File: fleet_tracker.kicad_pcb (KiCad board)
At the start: 2 copper layers, 80 x 70 mm, 21 parts, among them J1 DB128V-5.08-5P-GN-S, J2 2685Y-116CNG1SNA01, J3 2685Y-116CNG1SNA01, U2 TJA1051T/3/1J, U3 TSR 1-2450E

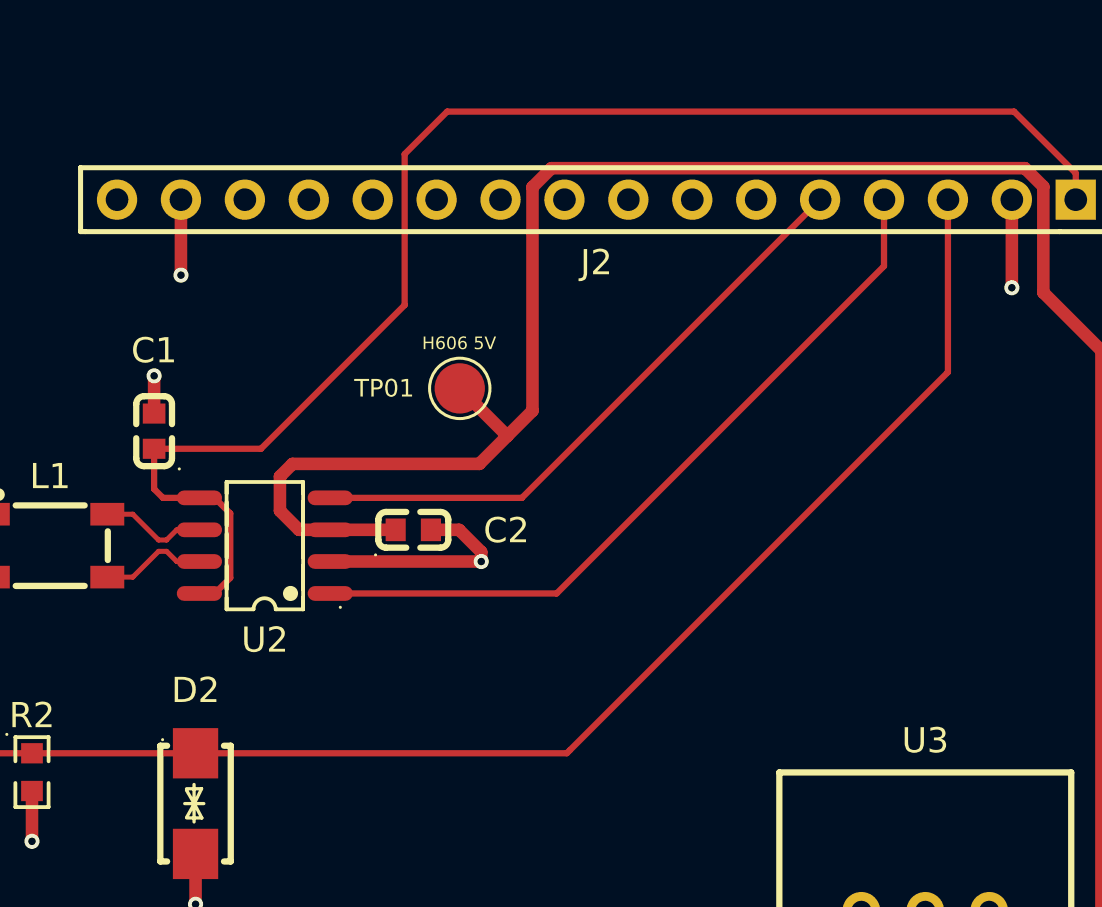
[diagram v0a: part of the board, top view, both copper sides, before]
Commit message: Post-cleanup: co-linear tracks merged, redundant vias removed
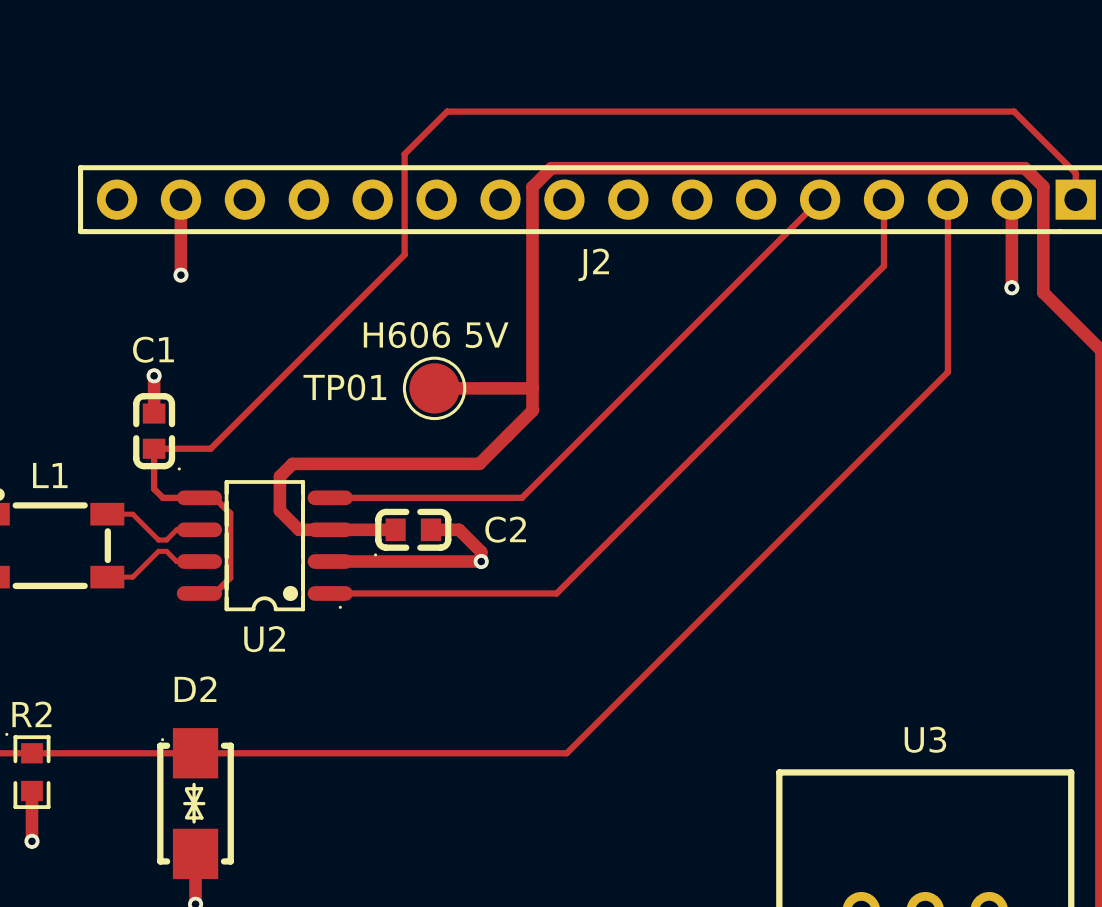
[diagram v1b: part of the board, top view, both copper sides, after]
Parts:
- moved TP01 1.00 mm to (142.5, 114.0)
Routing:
- net /+5V: track 90.4 -> 91.6 mm
- net +3.3V: track 56.8 -> 55.7 mm
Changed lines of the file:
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@@
 	(footprint "TestPoint:TestPoint_Pad_D2.0mm"
 		(layer "F.Cu")
-		(at 143.5 114)
+		(at 142.5 114)
 		(descr "SMD pad as test Point, diameter 2.0mm")
 		(tags "test point SMD pad")
 		(property "Reference" "TP01"
-			(at -3 0 0)
+			(at -3.5 0 0)
 			(layer "F.SilkS")
 			(effects
 				(font
-					(size 0.7 0.7)
-					(thickness 0.0875)
+					(size 1 1)
+					(thickness 0.125)
 				)
 			)
@@
 	)
 	(gr_text "H606 5V"
-		(at 142 112.5 0)
+		(at 142.5 112.5 0)
 		(layer "F.SilkS")
 		(effects
 			(font
-				(size 0.5 0.5)
-				(thickness 0.0625)
+				(size 1 1)
+				(thickness 0.15)
 			)
-			(justify left bottom)
+			(justify bottom)
 		)
 	)
@@
 	)
 	(segment
-		(start 167.98 105.45)
-		(end 165.53 103)
-		(width 0.25)
-		(layer "F.Cu")
-		(net 1)
-	)
-	(segment
-		(start 141.31 104.69)
-		(end 141.31 110.69)
+		(start 167.98 106.5)
+		(end 167.98 105.45)
 		(width 0.25)
 		(layer "F.Cu")
@@
 	)
 	(segment
-		(start 133.759749 122.15)
-		(end 134.379749 121.53)
+		(start 165.53 103)
+		(end 143 103)
 		(width 0.25)
 		(layer "F.Cu")
@@
 	)
 	(segment
-		(start 141.31 110.69)
-		(end 135.6 116.4)
+		(start 133.759749 122.15)
+		(end 134.379749 121.53)
 		(width 0.25)
 		(layer "F.Cu")
@@
 	)
 	(segment
-		(start 167.98 106.5)
-		(end 167.98 105.45)
+		(start 141.31 108.69)
+		(end 133.6 116.4)
 		(width 0.25)
 		(layer "F.Cu")
@@
 	)
 	(segment
-		(start 165.53 103)
-		(end 143 103)
+		(start 141.31 104.69)
+		(end 141.31 108.69)
 		(width 0.25)
 		(layer "F.Cu")
@@
 	)
 	(segment
+		(start 133.6 116.4)
+		(end 131.353749 116.4)
+		(width 0.25)
+		(layer "F.Cu")
+		(net 1)
+	)
+	(segment
 		(start 133.759749 118.35)
 		(end 133.153749 118.35)
@@
 	)
 	(segment
-		(start 133.153749 118.35)
-		(end 131.703749 118.35)
+		(start 167.98 105.45)
+		(end 165.53 103)
 		(width 0.25)
 		(layer "F.Cu")
@@
 	)
 	(segment
-		(start 135.6 116.4)
-		(end 131.353749 116.4)
+		(start 133.153749 118.35)
+		(end 131.703749 118.35)
 		(width 0.25)
 		(layer "F.Cu")
@@
 	)
 	(segment
+		(start 142.5 114)
+		(end 146.39 114)
+		(width 0.5)
+		(layer "F.Cu")
+		(net 3)
+	)
+	(segment
 		(start 169 136.5)
 		(end 167 138.5)
@@
 	)
 	(segment
-		(start 145.39 115.89)
-		(end 143.5 114)
+		(start 146.39 114.89)
+		(end 146.39 114)
 		(width 0.5)
 		(layer "F.Cu")
@@
 	)
 	(segment
-		(start 146.39 114.89)
+		(start 146.39 114)
 		(end 146.39 106.000818)
 		(width 0.5)
@@
 	)
 	(segment
-		(start 147.877293 128.377293)
+		(start 147.754586 128.5)
 		(end 162.9 113.354587)
 		(width 0.25)
@@
 	)
 	(segment
-		(start 147.754586 128.5)
-		(end 147.877293 128.377293)
-		(width 0.25)
-		(layer "F.Cu")
-		(net 5)
-	)
-	(segment
 		(start 113 124.08)
 		(end 117.629999 119.450001)
@@
 		(name "$teardrop_padvia$")
 		(hatch none 0.1)
-		(priority 30009)
+		(priority 30006)
 		(attr
 			(teardrop
@@
 		(polygon
 			(pts
-				(xy 121.553749 122.405764) (xy 121.053749 122.405764) (xy 121.009513 122.941473) (xy 121.303749 123.001)
-				(xy 121.597985 122.941473)
+				(xy 162.594236 144.25) (xy 162.594236 143.75) (xy 162.058527 143.705764) (xy 161.999 144) (xy 162.058527 144.294236)
 			)
 		)
@@
 		(name "$teardrop_padvia$")
 		(hatch none 0.1)
-		(priority 30003)
+		(priority 30010)
 		(attr
 			(teardrop
@@
 		(polygon
 			(pts
-				(xy 152.25 148.405764) (xy 151.75 148.405764) (xy 151.705764 148.941473) (xy 152 149.001) (xy 152.294236 148.941473)
+				(xy 165.69 109.405764) (xy 165.19 109.405764) (xy 165.145764 109.941473) (xy 165.44 110.001) (xy 165.734236 109.941473)
 			)
 		)
@@
 		(name "$teardrop_padvia$")
 		(hatch none 0.1)
-		(priority 30010)
+		(priority 30012)
 		(attr
 			(teardrop
@@
 		(polygon
 			(pts
-				(xy 165.69 109.405764) (xy 165.19 109.405764) (xy 165.145764 109.941473) (xy 165.44 110.001) (xy 165.734236 109.941473)
+				(xy 132.67 89.405764) (xy 132.17 89.405764) (xy 132.125764 89.941473) (xy 132.42 90.001) (xy 132.714236 89.941473)
 			)
 		)
@@
 		(name "$teardrop_padvia$")
 		(hatch none 0.1)
-		(priority 30006)
+		(priority 30007)
 		(attr
 			(teardrop
@@
 		(polygon
 			(pts
-				(xy 162.594236 144.25) (xy 162.594236 143.75) (xy 162.058527 143.705764) (xy 161.999 144) (xy 162.058527 144.294236)
+				(xy 162.25 143.405764) (xy 161.75 143.405764) (xy 161.705764 143.941473) (xy 162 144.001) (xy 162.294236 143.941473)
 			)
 		)
@@
 		(name "$teardrop_padvia$")
 		(hatch none 0.1)
-		(priority 30011)
+		(priority 30000)
 		(attr
 			(teardrop
@@
 		(polygon
 			(pts
-				(xy 132.67 108.905764) (xy 132.17 108.905764) (xy 132.125764 109.441473) (xy 132.42 109.501) (xy 132.714236 109.441473)
+				(xy 126.75 131.405764) (xy 126.25 131.405764) (xy 126.205764 131.941473) (xy 126.5 132.001) (xy 126.794236 131.941473)
 			)
 		)
@@
 		(name "$teardrop_padvia$")
 		(hatch none 0.1)
-		(priority 30001)
+		(priority 30009)
 		(attr
 			(teardrop
@@
 		(polygon
 			(pts
-				(xy 133.25 133.905764) (xy 132.75 133.905764) (xy 132.705764 134.441473) (xy 133 134.501) (xy 133.294236 134.441473)
+				(xy 121.553749 122.405764) (xy 121.053749 122.405764) (xy 121.009513 122.941473) (xy 121.303749 123.001)
+				(xy 121.597985 122.941473)
 			)
 		)
@@
 		(name "$teardrop_padvia$")
 		(hatch none 0.1)
-		(priority 30008)
+		(priority 30004)
 		(attr
 			(teardrop
@@
 		(polygon
 			(pts
-				(xy 143.759513 120.63) (xy 143.759513 121.13) (xy 144.295222 121.174236) (xy 144.354749 120.88)
-				(xy 144.295222 120.585764)
+				(xy 131.103749 114.094236) (xy 131.603749 114.094236) (xy 131.647985 113.558527) (xy 131.353749 113.499)
+				(xy 131.059513 113.558527)
 			)
 		)
@@
 		(name "$teardrop_padvia$")
 		(hatch none 0.1)
-		(priority 30004)
+		(priority 30008)
 		(attr
 			(teardrop
@@
 		(polygon
 			(pts
-				(xy 131.103749 114.094236) (xy 131.603749 114.094236) (xy 131.647985 113.558527) (xy 131.353749 113.499)
-				(xy 131.059513 113.558527)
+				(xy 143.759513 120.63) (xy 143.759513 121.13) (xy 144.295222 121.174236) (xy 144.354749 120.88)
+				(xy 144.295222 120.585764)
 			)
 		)
@@
 		(name "$teardrop_padvia$")
 		(hatch none 0.1)
-		(priority 30007)
+		(priority 30003)
 		(attr
 			(teardrop
@@
 		(polygon
 			(pts
-				(xy 162.25 143.405764) (xy 161.75 143.405764) (xy 161.705764 143.941473) (xy 162 144.001) (xy 162.294236 143.941473)
+				(xy 152.25 148.405764) (xy 151.75 148.405764) (xy 151.705764 148.941473) (xy 152 149.001) (xy 152.294236 148.941473)
 			)
 		)
@@
 		(name "$teardrop_padvia$")
 		(hatch none 0.1)
-		(priority 30013)
+		(priority 30001)
 		(attr
 			(teardrop
@@
 		(polygon
 			(pts
-				(xy 144.379037 120.171736) (xy 144.025485 120.525288) (xy 144.059513 120.938527) (xy 144.354456 120.880707)
-				(xy 144.647985 120.821473)
+				(xy 133.25 133.905764) (xy 132.75 133.905764) (xy 132.705764 134.441473) (xy 133 134.501) (xy 133.294236 134.441473)
 			)
 		)
@@
 		(name "$teardrop_padvia$")
 		(hatch none 0.1)
-		(priority 30012)
+		(priority 30013)
 		(attr
 			(teardrop
@@
 		(polygon
 			(pts
-				(xy 132.67 89.405764) (xy 132.17 89.405764) (xy 132.125764 89.941473) (xy 132.42 90.001) (xy 132.714236 89.941473)
+				(xy 144.379037 120.171736) (xy 144.025485 120.525288) (xy 144.059513 120.938527) (xy 144.354456 120.880707)
+				(xy 144.647985 120.821473)
 			)
 		)
@@
 		(net_name "GND")
 		(layer "F.Cu")
-		(hatch edge 0.5)
-		(connect_pads
-			(clearance 0.5)
+		(name "$teardrop_padvia$")
+		(hatch none 0.1)
+		(priority 30011)
+		(attr
+			(teardrop
+				(type padvia)
+			)
 		)
-		(min_thickness 0.25)
+		(connect_pads yes
+			(clearance 0)
+		)
+		(min_thickness 0.0254)
 		(filled_areas_thickness no)
 		(fill yes
 			(thermal_gap 0.5)
 			(thermal_bridge_width 0.5)
+			(island_removal_mode 1)
+			(island_area_min 10)
 		)
 		(polygon
 			(pts
-				(xy 185 80) (xy 105 80) (xy 105 150) (xy 185 150)
+				(xy 132.67 108.905764) (xy 132.17 108.905764) (xy 132.125764 109.441473) (xy 132.42 109.501) (xy 132.714236 109.441473)
 			)
 		)
@@
 		(net_name "GND")
 		(layer "F.Cu")
-		(name "$teardrop_padvia$")
-		(hatch none 0.1)
-		(priority 30000)
-		(attr
-			(teardrop
-				(type padvia)
-			)
-		)
-		(connect_pads yes
-			(clearance 0)
+		(hatch edge 0.5)
+		(connect_pads
+			(clearance 0.5)
 		)
-		(min_thickness 0.0254)
+		(min_thickness 0.25)
 		(filled_areas_thickness no)
 		(fill yes
 			(thermal_gap 0.5)
 			(thermal_bridge_width 0.5)
-			(island_removal_mode 1)
-			(island_area_min 10)
 		)
 		(polygon
 			(pts
-				(xy 126.75 131.405764) (xy 126.25 131.405764) (xy 126.205764 131.941473) (xy 126.5 132.001) (xy 126.794236 131.941473)
+				(xy 185 80) (xy 105 80) (xy 105 150) (xy 185 150)
 			)
 		)

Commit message: pcb: add silkscren labels for j1
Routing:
- net +3.3V: track 55.7 -> 54.8 mm
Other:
- board text added: "+24V"
- board text added: "CAN_H"
- board text added: "CAN_L"
- board text added: "GND"
- board text added: "IGN"
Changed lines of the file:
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@@
 		(at 113 124.08 -90)
 		(property "Reference" "J1"
-			(at 0.92 6.5 90)
+			(at -14.08 0 0)
 			(layer "F.SilkS")
 			(effects
@@
 		(layer "Edge.Cuts")
 	)
+	(gr_text "IGN"
+		(at 107 129.16 90)
+		(layer "F.SilkS")
+		(effects
+			(font
+				(size 1 1)
+				(thickness 0.1)
+			)
+			(justify bottom)
+		)
+	)
+	(gr_text "CAN_L"
+		(at 107 119 90)
+		(layer "F.SilkS")
+		(effects
+			(font
+				(size 1 1)
+				(thickness 0.1)
+			)
+			(justify bottom)
+		)
+	)
+	(gr_text "CAN_H"
+		(at 107 124.08 90)
+		(layer "F.SilkS")
+		(effects
+			(font
+				(size 1 1)
+				(thickness 0.1)
+			)
+			(justify bottom)
+		)
+	)
 	(gr_text "H606 5V"
 		(at 142.5 112.5 0)
@@
 				(size 1 1)
 				(thickness 0.15)
+			)
+			(justify bottom)
+		)
+	)
+	(gr_text "GND"
+		(at 107 113.92 90)
+		(layer "F.SilkS")
+		(effects
+			(font
+				(size 1 1)
+				(thickness 0.1)
 			)
 			(justify bottom)
@@
 		)
 	)
+	(gr_text "+24V"
+		(at 107 134.24 90)
+		(layer "F.SilkS")
+		(effects
+			(font
+				(size 1 1)
+				(thickness 0.1)
+			)
+			(justify bottom)
+		)
+	)
 	(gr_text "XCOPE AI"
 		(at 109.5 109 90)
@@
 	)
 	(segment
-		(start 143 103)
-		(end 141.31 104.69)
+		(start 141.31 108.69)
+		(end 133.6 116.4)
+		(width 0.25)
+		(layer "F.Cu")
+		(net 1)
+	)
+	(segment
+		(start 131.703749 118.35)
+		(end 131.353749 118)
+		(width 0.25)
+		(layer "F.Cu")
+		(net 1)
+	)
+	(segment
+		(start 133.759749 122.15)
+		(end 134.379749 121.53)
 		(width 0.25)
 		(layer "F.Cu")
@@
 	)
 	(segment
-		(start 131.703749 118.35)
-		(end 131.353749 118)
-		(width 0.25)
-		(layer "F.Cu")
-		(net 1)
-	)
-	(segment
-		(start 165.53 103)
-		(end 143 103)
-		(width 0.25)
-		(layer "F.Cu")
-		(net 1)
-	)
-	(segment
-		(start 133.759749 122.15)
-		(end 134.379749 121.53)
-		(width 0.25)
-		(layer "F.Cu")
-		(net 1)
-	)
-	(segment
 		(start 131.353749 118)
 		(end 131.353749 116.4)
@@
 	)
 	(segment
-		(start 141.31 108.69)
-		(end 133.6 116.4)
+		(start 167.98 105.45)
+		(end 166.53 104)
+		(width 0.25)
+		(layer "F.Cu")
+		(net 1)
+	)
+	(segment
+		(start 142 104)
+		(end 141.31 104.69)
+		(width 0.25)
+		(layer "F.Cu")
+		(net 1)
+	)
+	(segment
+		(start 134.379749 121.53)
+		(end 134.379749 118.97)
 		(width 0.25)
 		(layer "F.Cu")
@@
 	)
 	(segment
-		(start 134.379749 121.53)
-		(end 134.379749 118.97)
+		(start 133.759749 118.35)
+		(end 133.153749 118.35)
+		(width 0.25)
+		(layer "F.Cu")
+		(net 1)
+	)
+	(segment
+		(start 133.153749 122.15)
+		(end 133.759749 122.15)
+		(width 0.25)
+		(layer "F.Cu")
+		(net 1)
+	)
+	(segment
+		(start 133.153749 118.35)
+		(end 131.703749 118.35)
+		(width 0.25)
+		(layer "F.Cu")
+		(net 1)
+	)
+	(segment
+		(start 166.53 104)
+		(end 142 104)
 		(width 0.25)
 		(layer "F.Cu")
@@
 		(start 133.6 116.4)
 		(end 131.353749 116.4)
-		(width 0.25)
-		(layer "F.Cu")
-		(net 1)
-	)
-	(segment
-		(start 133.759749 118.35)
-		(end 133.153749 118.35)
-		(width 0.25)
-		(layer "F.Cu")
-		(net 1)
-	)
-	(segment
-		(start 133.153749 122.15)
-		(end 133.759749 122.15)
-		(width 0.25)
-		(layer "F.Cu")
-		(net 1)
-	)
-	(segment
-		(start 167.98 105.45)
-		(end 165.53 103)
-		(width 0.25)
-		(layer "F.Cu")
-		(net 1)
-	)
-	(segment
-		(start 133.153749 118.35)
-		(end 131.703749 118.35)
 		(width 0.25)
 		(layer "F.Cu")
@@
 		(name "$teardrop_padvia$")
 		(hatch none 0.1)
-		(priority 30006)
+		(priority 30003)
 		(attr
 			(teardrop
@@
 		(polygon
 			(pts
-				(xy 162.594236 144.25) (xy 162.594236 143.75) (xy 162.058527 143.705764) (xy 161.999 144) (xy 162.058527 144.294236)
+				(xy 152.25 148.405764) (xy 151.75 148.405764) (xy 151.705764 148.941473) (xy 152 149.001) (xy 152.294236 148.941473)
 			)
 		)
@@
 		(name "$teardrop_padvia$")
 		(hatch none 0.1)
-		(priority 30005)
+		(priority 30008)
 		(attr
 			(teardrop
@@
 		(polygon
 			(pts
-				(xy 161.405764 143.75) (xy 161.405764 144.25) (xy 161.941473 144.294236) (xy 162.001 144) (xy 161.941473 143.705764)
+				(xy 143.759513 120.63) (xy 143.759513 121.13) (xy 144.295222 121.174236) (xy 144.354749 120.88)
+				(xy 144.295222 120.585764)
 			)
 		)
@@
 		(name "$teardrop_padvia$")
 		(hatch none 0.1)
-		(priority 30002)
+		(priority 30001)
 		(attr
 			(teardrop
@@
 		(polygon
 			(pts
-				(xy 118.405764 113.67) (xy 118.405764 114.17) (xy 118.941473 114.214236) (xy 119.001 113.92) (xy 118.941473 113.625764)
+				(xy 133.25 133.905764) (xy 132.75 133.905764) (xy 132.705764 134.441473) (xy 133 134.501) (xy 133.294236 134.441473)
 			)
 		)
@@
 		(name "$teardrop_padvia$")
 		(hatch none 0.1)
-		(priority 30010)
+		(priority 30007)
 		(attr
 			(teardrop
@@
 		(polygon
 			(pts
-				(xy 165.69 109.405764) (xy 165.19 109.405764) (xy 165.145764 109.941473) (xy 165.44 110.001) (xy 165.734236 109.941473)
+				(xy 162.25 143.405764) (xy 161.75 143.405764) (xy 161.705764 143.941473) (xy 162 144.001) (xy 162.294236 143.941473)
 			)
 		)
@@
 		(name "$teardrop_padvia$")
 		(hatch none 0.1)
-		(priority 30012)
+		(priority 30004)
 		(attr
 			(teardrop
@@
 		(polygon
 			(pts
-				(xy 132.67 89.405764) (xy 132.17 89.405764) (xy 132.125764 89.941473) (xy 132.42 90.001) (xy 132.714236 89.941473)
+				(xy 131.103749 114.094236) (xy 131.603749 114.094236) (xy 131.647985 113.558527) (xy 131.353749 113.499)
+				(xy 131.059513 113.558527)
 			)
 		)
@@
 		(name "$teardrop_padvia$")
 		(hatch none 0.1)
-		(priority 30007)
+		(priority 30010)
 		(attr
 			(teardrop
@@
 		(polygon
 			(pts
-				(xy 162.25 143.405764) (xy 161.75 143.405764) (xy 161.705764 143.941473) (xy 162 144.001) (xy 162.294236 143.941473)
+				(xy 165.69 109.405764) (xy 165.19 109.405764) (xy 165.145764 109.941473) (xy 165.44 110.001) (xy 165.734236 109.941473)
 			)
 		)
@@
 		(name "$teardrop_padvia$")
 		(hatch none 0.1)
-		(priority 30000)
+		(priority 30011)
 		(attr
 			(teardrop
@@
 		(polygon
 			(pts
-				(xy 126.75 131.405764) (xy 126.25 131.405764) (xy 126.205764 131.941473) (xy 126.5 132.001) (xy 126.794236 131.941473)
+				(xy 132.67 108.905764) (xy 132.17 108.905764) (xy 132.125764 109.441473) (xy 132.42 109.501) (xy 132.714236 109.441473)
 			)
 		)
@@
 		(name "$teardrop_padvia$")
 		(hatch none 0.1)
-		(priority 30009)
+		(priority 30013)
 		(attr
 			(teardrop
@@
 		(polygon
 			(pts
-				(xy 121.553749 122.405764) (xy 121.053749 122.405764) (xy 121.009513 122.941473) (xy 121.303749 123.001)
-				(xy 121.597985 122.941473)
+				(xy 144.379037 120.171736) (xy 144.025485 120.525288) (xy 144.059513 120.938527) (xy 144.354456 120.880707)
+				(xy 144.647985 120.821473)
 			)
 		)
@@
 		(name "$teardrop_padvia$")
 		(hatch none 0.1)
-		(priority 30004)
+		(priority 30006)
 		(attr
 			(teardrop
@@
 		(polygon
 			(pts
-				(xy 131.103749 114.094236) (xy 131.603749 114.094236) (xy 131.647985 113.558527) (xy 131.353749 113.499)
-				(xy 131.059513 113.558527)
+				(xy 162.594236 144.25) (xy 162.594236 143.75) (xy 162.058527 143.705764) (xy 161.999 144) (xy 162.058527 144.294236)
 			)
 		)
@@
 		(name "$teardrop_padvia$")
 		(hatch none 0.1)
-		(priority 30008)
+		(priority 30000)
 		(attr
 			(teardrop
@@
 		(polygon
 			(pts
-				(xy 143.759513 120.63) (xy 143.759513 121.13) (xy 144.295222 121.174236) (xy 144.354749 120.88)
-				(xy 144.295222 120.585764)
+				(xy 126.75 131.405764) (xy 126.25 131.405764) (xy 126.205764 131.941473) (xy 126.5 132.001) (xy 126.794236 131.941473)
 			)
 		)
@@
 		(name "$teardrop_padvia$")
 		(hatch none 0.1)
-		(priority 30003)
+		(priority 30009)
 		(attr
 			(teardrop
@@
 		(polygon
 			(pts
-				(xy 152.25 148.405764) (xy 151.75 148.405764) (xy 151.705764 148.941473) (xy 152 149.001) (xy 152.294236 148.941473)
+				(xy 121.553749 122.405764) (xy 121.053749 122.405764) (xy 121.009513 122.941473) (xy 121.303749 123.001)
+				(xy 121.597985 122.941473)
 			)
 		)
@@
 		(name "$teardrop_padvia$")
 		(hatch none 0.1)
-		(priority 30001)
+		(priority 30012)
 		(attr
 			(teardrop
@@
 		(polygon
 			(pts
-				(xy 133.25 133.905764) (xy 132.75 133.905764) (xy 132.705764 134.441473) (xy 133 134.501) (xy 133.294236 134.441473)
+				(xy 132.67 89.405764) (xy 132.17 89.405764) (xy 132.125764 89.941473) (xy 132.42 90.001) (xy 132.714236 89.941473)
 			)
 		)
@@
 		(name "$teardrop_padvia$")
 		(hatch none 0.1)
-		(priority 30013)
+		(priority 30002)
 		(attr
 			(teardrop
@@
 		(polygon
 			(pts
-				(xy 144.379037 120.171736) (xy 144.025485 120.525288) (xy 144.059513 120.938527) (xy 144.354456 120.880707)
-				(xy 144.647985 120.821473)
+				(xy 118.405764 113.67) (xy 118.405764 114.17) (xy 118.941473 114.214236) (xy 119.001 113.92) (xy 118.941473 113.625764)
 			)
 		)
@@
 		(name "$teardrop_padvia$")
 		(hatch none 0.1)
-		(priority 30011)
+		(priority 30005)
 		(attr
 			(teardrop
@@
 		(polygon
 			(pts
-				(xy 132.67 108.905764) (xy 132.17 108.905764) (xy 132.125764 109.441473) (xy 132.42 109.501) (xy 132.714236 109.441473)
-			)
-		)
+				(xy 161.405764 143.75) (xy 161.405764 144.25) (xy 161.941473 144.294236) (xy 162.001 144) (xy 161.941473 143.705764)
+			)
+		)
